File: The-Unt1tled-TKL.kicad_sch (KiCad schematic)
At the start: 194 parts, among them J1 USB_C_Receptacle_USB2.0, SW1 SW_Push, U1 ATmega32U4-A, Y1 16MHz

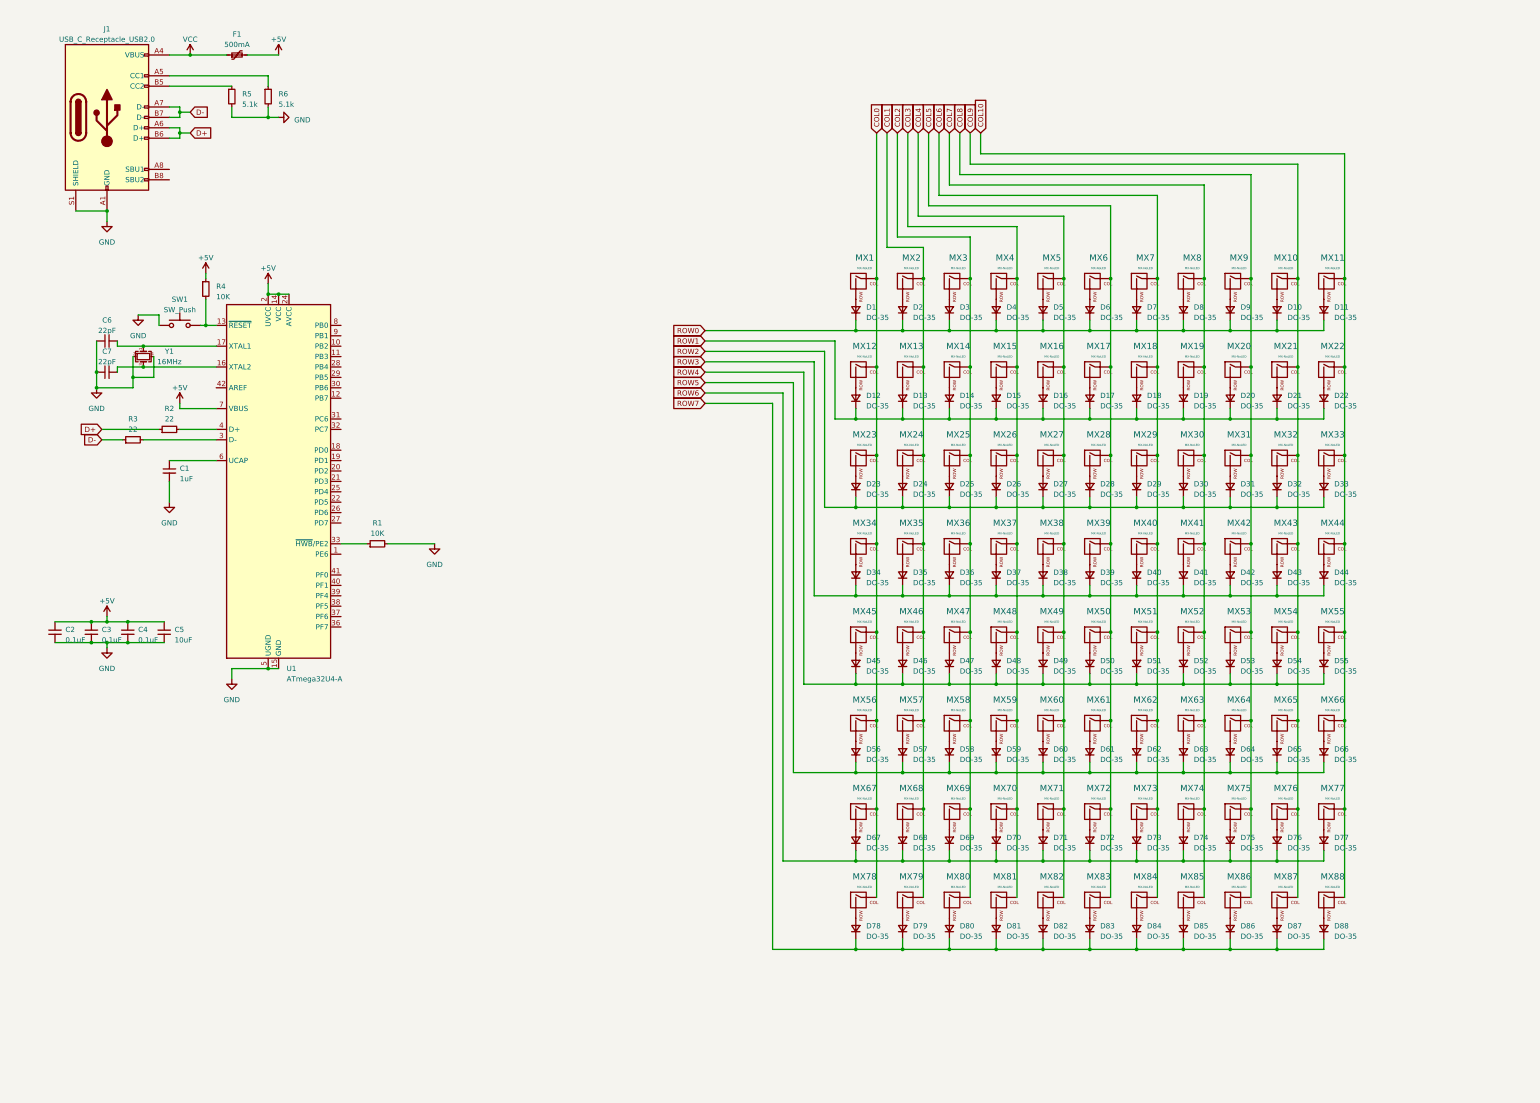
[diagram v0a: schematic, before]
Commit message: Re-did Whole Schematic
I redesigned the whole PCB schematic to support ISO and ANSI. I also changed the microcontroller to one with more pins for row/col layout. Instead I'm using an ATmega324A-P. This requires the use of v-usb.
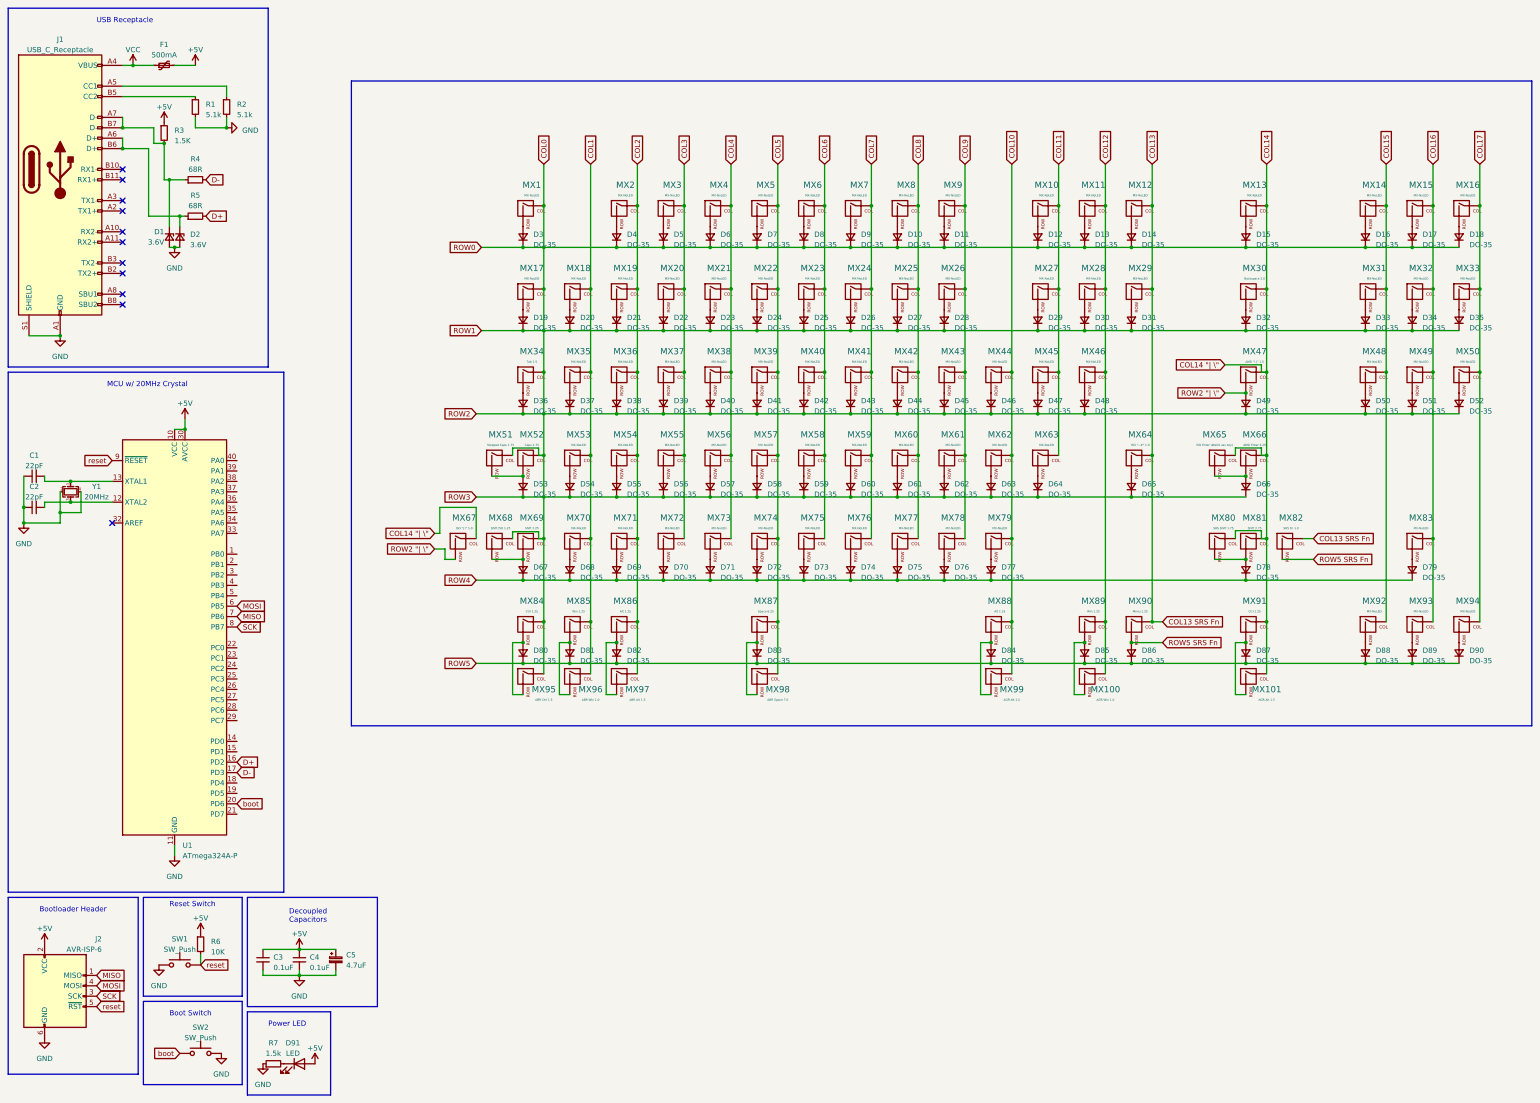
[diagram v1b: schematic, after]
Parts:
- removed C5: 10uF, Capacitor_THT:CP_Radial_D4.0mm_P1.50mm, symbol Device:C_Small
- removed C6, C7: 22pF, Capacitor_THT:C_Disc_D5.0mm_W2.5mm_P2.50mm, symbol Device:C_Small
- removed D1, D2: DO-35, Diode_THT:D_DO-35_SOD27_P7.62mm_Horizontal, symbol Device:D_Small
- removed J1: USB_C_Receptacle_USB2.0, Connector_USB:USB_C_Receptacle_G-Switch_GT-USB-7010ASV, symbol Connector:USB_C_Receptacle_USB2.0
- removed U1: ATmega32U4-A, Package_QFP:TQFP-44_10x10mm_P0.8mm, symbol MCU_Microchip_ATmega:ATmega32U4-A
- added C5: 4.7uF, symbol Device:C_Polarized_Small
- added D1, D2: 3.6V, symbol Device:D_Zener_Small
- added D89, D90: DO-35, Diode_THT:D_DO-35_SOD27_P7.62mm_Horizontal, symbol Device:D_Small
- added D91: LED, symbol Device:LED
- added J1: USB_C_Receptacle, symbol Connector:USB_C_Receptacle
- added J2: AVR-ISP-6, symbol Connector:AVR-ISP-6
- added MX100: AGR Win 1.0, MX_Alps_Hybrid:MX-1U-NoLED, symbol MX_Alps_Hybrid:MX-NoLED
- added MX101, MX99: AGR Alt 1.5, MX_Alps_Hybrid:MX-1U-NoLED, symbol MX_Alps_Hybrid:MX-NoLED
- added MX89: Win 1.25, MX_Alps_Hybrid:MX-1U-NoLED, symbol MX_Alps_Hybrid:MX-NoLED
- added MX90: Menu 1.25, MX_Alps_Hybrid:MX-1U-NoLED, symbol MX_Alps_Hybrid:MX-NoLED
- added MX91: Ctrl 1.25, MX_Alps_Hybrid:MX-1U-NoLED, symbol MX_Alps_Hybrid:MX-NoLED
- added MX92, MX93, MX94: MX-NoLED, MX_Alps_Hybrid:MX-1U-NoLED, symbol MX_Alps_Hybrid:MX-NoLED
- added MX95: ABR Ctrl 1.5, MX_Alps_Hybrid:MX-1U-NoLED, symbol MX_Alps_Hybrid:MX-NoLED
- added MX96: ABR Win 1.0, MX_Alps_Hybrid:MX-1U-NoLED, symbol MX_Alps_Hybrid:MX-NoLED
- added MX97: ABR Alt 1.5, MX_Alps_Hybrid:MX-1U-NoLED, symbol MX_Alps_Hybrid:MX-NoLED
- added MX98: ABR Space 7.0, MX_Alps_Hybrid:MX-1U-NoLED, symbol MX_Alps_Hybrid:MX-NoLED
- added R7: 1.5k, symbol Device:R_Small
- added SW2: SW_Push, symbol Switch:SW_Push
- added U1: ATmega324A-P, Package_DIP:DIP-40_W15.24mm, symbol MCU_Microchip_ATmega:ATmega324A-P
- C1: value 1uF -> 22pF; footprint Capacitor_THT:CP_Radial_D4.0mm_P1.50mm -> Capacitor_THT:C_Disc_D5.0mm_W2.5mm_P2.50mm
- C2: value 0.1uF -> 22pF; footprint Capacitor_THT:CP_Radial_D5.0mm_P2.00mm -> Capacitor_THT:C_Disc_D5.0mm_W2.5mm_P2.50mm
- MX30: value MX-NoLED -> Backspace 2.0
- MX34: value MX-NoLED -> Tab 1.5
- MX47: value MX-NoLED -> ANSI "\ |" 1.5
- MX51: value MX-NoLED -> Stepped Caps 1.75
- MX52: value MX-NoLED -> Caps 1.75
- MX64: value MX-NoLED -> ISO "~#" 1.0
- MX65: value MX-NoLED -> ISO Enter (Weird ass key)
- MX66: value MX-NoLED -> ANSI Enter 2.25
- MX67: value MX-NoLED -> ISO "| \" 1.0
- MX68: value MX-NoLED -> Shift ISO 1.25
- MX69: value MX-NoLED -> Shift 2.25
- MX73, MX74, MX75, MX76, MX77, MX78, MX79: footprint MX_Alps_Hybrid:MX-1.25U-NoLED -> MX_Alps_Hybrid:MX-1U-NoLED
- MX80: value MX-NoLED -> SRS Shift 1.75; footprint MX_Alps_Hybrid:MX-1.5U-NoLED -> MX_Alps_Hybrid:MX-1U-NoLED
- MX81: value MX-NoLED -> Shift 2.75; footprint MX_Alps_Hybrid:MX-1.5U-NoLED -> MX_Alps_Hybrid:MX-1U-NoLED
- MX82: value MX-NoLED -> SRS Fn 1.0; footprint MX_Alps_Hybrid:MX-1.75U-NoLED -> MX_Alps_Hybrid:MX-1U-NoLED
- MX83: footprint MX_Alps_Hybrid:MX-2U-NoLED -> MX_Alps_Hybrid:MX-1U-NoLED
- MX84: value MX-NoLED -> Ctrl 1.25; footprint MX_Alps_Hybrid:MX-2.25U-NoLED -> MX_Alps_Hybrid:MX-1U-NoLED
- MX85: value MX-NoLED -> Win 1.25; footprint MX_Alps_Hybrid:MX-2.25U-NoLED -> MX_Alps_Hybrid:MX-1U-NoLED
- MX86: value MX-NoLED -> Alt 1.25; footprint MX_Alps_Hybrid:MX-2.25U-NoLED -> MX_Alps_Hybrid:MX-1U-NoLED
- MX87: value MX-NoLED -> Space 6.25; footprint MX_Alps_Hybrid:MX-2.75U-NoLED -> MX_Alps_Hybrid:MX-1U-NoLED
- MX88: value MX-NoLED -> Alt 1.25; footprint MX_Alps_Hybrid:MX-6.25U-NoLED -> MX_Alps_Hybrid:MX-1U-NoLED
- R1: value 10K -> 5.1k
- R2: value 22 -> 5.1k
- R3: value 22 -> 1.5K; footprint Resistor_THT:R_Axial_DIN0207_L6.3mm_D2.5mm_P7.62mm_Horizontal -> (none)
- R4: value 10K -> 68R
- R5: value 5.1k -> 68R
- R6: value 5.1k -> 10K
- Y1: value 16MHz -> 20MHz
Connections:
- net ROW0 is gone; now on net COL0: D10.1 (K), D11.1 (K), D3.1 (K), D4.1 (K), D5.1 (K), D6.1 (K), D7.1 (K), D8.1 (K), D9.1 (K)
- net ROW1 is gone; now on net COL0: D12.1 (K), D13.1 (K), D14.1 (K), D15.1 (K), D16.1 (K), D17.1 (K), D18.1 (K), D19.1 (K), D20.1 (K), D21.1 (K), D22.1 (K)
- net ROW2 is gone; now on net COL0: D23.1 (K), D24.1 (K), D25.1 (K), D26.1 (K), D27.1 (K), D28.1 (K), D29.1 (K), D30.1 (K), D31.1 (K), D32.1 (K), D33.1 (K)
- net ROW3 is gone; now on net COL0: D34.1 (K), D35.1 (K), D36.1 (K), D37.1 (K), D38.1 (K), D39.1 (K), D40.1 (K), D41.1 (K), D42.1 (K), D43.1 (K), D44.1 (K)
- net ROW6 is gone; now on net ROW4: D67.1 (K), D68.1 (K), D69.1 (K), D70.1 (K), D71.1 (K), D72.1 (K), D73.1 (K), D74.1 (K), D75.1 (K), D76.1 (K), D77.1 (K)
- net +5V: now also R3.1, R6.1, C5.1, D91.2 (A), J2.2 (VCC), U1.10 (VCC), U1.30 (AVCC); no longer C2.1, R4.1
- net COL0: now also D45.1 (K), D46.1 (K), D47.1 (K), D48.1 (K), D49.1 (K), D50.1 (K), D51.1 (K), D52.1 (K), D53.1 (K), D54.1 (K), D55.1 (K), D56.1 (K), D57.1 (K), D58.1 (K), D59.1 (K), D60.1 (K), D61.1 (K), D62.1 (K), D63.1 (K), D64.1 (K), D65.1 (K), D66.1 (K), MX17.1 (COL), MX51.1 (COL), MX52.1 (COL), MX68.1 (COL), MX69.1 (COL), MX84.1 (COL), MX95.1 (COL); no longer MX12.1 (COL), MX23.1 (COL), MX45.1 (COL), MX56.1 (COL), MX67.1 (COL), MX78.1 (COL)
- net COL1: now also MX18.1 (COL), MX53.1 (COL), MX70.1 (COL), MX85.1 (COL), MX96.1 (COL); no longer MX13.1 (COL), MX2.1 (COL), MX24.1 (COL), MX46.1 (COL), MX57.1 (COL), MX68.1 (COL), MX79.1 (COL)
- net COL10: now also MX62.1 (COL), MX79.1 (COL), MX99.1 (COL); no longer MX11.1 (COL), MX22.1 (COL), MX33.1 (COL), MX55.1 (COL), MX66.1 (COL), MX77.1 (COL)
- net COL2: now also MX19.1 (COL), MX2.1 (COL), MX54.1 (COL), MX71.1 (COL), MX86.1 (COL), MX97.1 (COL); no longer MX14.1 (COL), MX25.1 (COL), MX3.1 (COL), MX47.1 (COL), MX58.1 (COL), MX69.1 (COL), MX80.1 (COL)
- net COL3: now also MX20.1 (COL), MX3.1 (COL), MX55.1 (COL), MX72.1 (COL); no longer MX15.1 (COL), MX26.1 (COL), MX4.1 (COL), MX48.1 (COL), MX59.1 (COL), MX70.1 (COL), MX81.1 (COL)
- net COL4: now also MX21.1 (COL), MX4.1 (COL), MX56.1 (COL), MX73.1 (COL); no longer MX16.1 (COL), MX27.1 (COL), MX49.1 (COL), MX5.1 (COL), MX60.1 (COL), MX71.1 (COL), MX82.1 (COL)
- net COL5: now also MX22.1 (COL), MX5.1 (COL), MX57.1 (COL), MX74.1 (COL), MX87.1 (COL), MX98.1 (COL); no longer MX17.1 (COL), MX28.1 (COL), MX50.1 (COL), MX6.1 (COL), MX61.1 (COL), MX72.1 (COL), MX83.1 (COL)
- net COL6: now also MX23.1 (COL), MX58.1 (COL), MX6.1 (COL), MX75.1 (COL); no longer MX18.1 (COL), MX29.1 (COL), MX51.1 (COL), MX62.1 (COL), MX7.1 (COL), MX73.1 (COL), MX84.1 (COL)
- net COL7: now also MX24.1 (COL), MX59.1 (COL), MX7.1 (COL), MX76.1 (COL); no longer MX19.1 (COL), MX30.1 (COL), MX52.1 (COL), MX63.1 (COL), MX74.1 (COL), MX8.1 (COL), MX85.1 (COL)
- net COL8: now also MX25.1 (COL), MX60.1 (COL), MX77.1 (COL), MX8.1 (COL); no longer MX20.1 (COL), MX31.1 (COL), MX53.1 (COL), MX64.1 (COL), MX75.1 (COL), MX86.1 (COL), MX9.1 (COL)
- net COL9: now also MX26.1 (COL), MX61.1 (COL), MX78.1 (COL), MX9.1 (COL); no longer MX10.1 (COL), MX21.1 (COL), MX32.1 (COL), MX54.1 (COL), MX65.1 (COL), MX76.1 (COL), MX87.1 (COL)
- net D+: now also R5.2, U1.16 (PD2); no longer R2.1
- net D-: now also R4.2, U1.17 (PD3); no longer R3.1
- net GND: now also C1.1, C2.1, R2.2, C5.2, D1.2 (A), D2.2 (A), J1.A1 (GND), J1.A12 (GND), J1.B1 (GND), J1.B12 (GND), J1.S1 (SHIELD), J2.6 (GND), R7.1, SW2.2, U1.11 (GND), U1.31 (GND); no longer C1.2, C2.2, R5.2, R6.2
- net ROW4: now also D78.1 (K), D79.1 (K); no longer D45.1 (K), D46.1 (K), D47.1 (K), D48.1 (K), D49.1 (K), D50.1 (K), D51.1 (K), D52.1 (K), D53.1 (K), D54.1 (K), D55.1 (K)
- net ROW5: now also D80.1 (K), D81.1 (K), D82.1 (K), D83.1 (K), D84.1 (K), D85.1 (K), D86.1 (K), D87.1 (K), D88.1 (K), D89.1 (K), D90.1 (K); no longer D56.1 (K), D57.1 (K), D58.1 (K), D59.1 (K), D60.1 (K), D61.1 (K), D62.1 (K), D63.1 (K), D64.1 (K), D65.1 (K), D66.1 (K)
- net VCC: now also J1.A4 (VBUS), J1.A9 (VBUS), J1.B4 (VBUS), J1.B9 (VBUS)
- net at MX40.2 (ROW): now also D42.2 (A); no longer D40.2 (A)
- net at D77.2 (A): now also MX79.2 (ROW); no longer MX77.2 (ROW)
- net at MX36.2 (ROW): now also D38.2 (A); no longer D36.2 (A)
- net at D61.2 (A): now also MX60.2 (ROW); no longer MX61.2 (ROW)
- net at D74.2 (A): now also MX76.2 (ROW); no longer MX74.2 (ROW)
- net at MX38.2 (ROW): now also D40.2 (A); no longer D38.2 (A)
- net at MX1.2 (ROW): now also D3.2 (A)
- net at MX58.2 (ROW): now also D59.2 (A); no longer D58.2 (A)
- net at D79.2 (A): now also MX83.2 (ROW); no longer MX79.2 (ROW)
- net at D6.2 (A): now also MX4.2 (ROW); no longer MX6.2 (ROW)
- net at D82.2 (A): now also MX86.2 (ROW), MX97.2 (ROW); no longer MX82.2 (ROW)
- net at D60.2 (A): now also MX59.2 (ROW); no longer MX60.2 (ROW)
- net at MX56.2 (ROW): now also D57.2 (A); no longer D56.2 (A)
- net at MX8.2 (ROW): now also D10.2 (A); no longer D8.2 (A)
- net at MX50.2 (ROW): now also D52.2 (A); no longer D50.2 (A)
- net at D83.2 (A): now also MX87.2 (ROW), MX98.2 (ROW); no longer MX83.2 (ROW)
- net at MX22.2 (ROW): now also D24.2 (A); no longer D22.2 (A)
- net at MX39.2 (ROW): now also D41.2 (A); no longer D39.2 (A)
- net at MX75.2 (ROW): now also D73.2 (A); no longer D75.2 (A)
- net at D47.2 (A): now also MX45.2 (ROW); no longer MX47.2 (ROW)
- net at MX43.2 (ROW): now also D45.2 (A); no longer D43.2 (A)
- net at MX10.2 (ROW): now also D12.2 (A); no longer D10.2 (A)
- net at D64.2 (A): now also MX63.2 (ROW); no longer MX64.2 (ROW)
- net at D81.2 (A): now also MX85.2 (ROW), MX96.2 (ROW); no longer MX81.2 (ROW)
- net at D46.2 (A): now also MX44.2 (ROW); no longer MX46.2 (ROW)
- net at MX41.2 (ROW): now also D43.2 (A); no longer D41.2 (A)
- net at MX24.2 (ROW): now also D26.2 (A); no longer D24.2 (A)
- net at MX14.2 (ROW): now also D16.2 (A); no longer D14.2 (A)
- net at D28.2 (A): now also MX26.2 (ROW); no longer MX28.2 (ROW)
- net at D9.2 (A): now also MX7.2 (ROW); no longer MX9.2 (ROW)
- net at MX35.2 (ROW): now also D37.2 (A); no longer D35.2 (A)
- net at MX17.2 (ROW): now also D19.2 (A); no longer D17.2 (A)
- net at MX73.2 (ROW): now also D71.2 (A); no longer D73.2 (A)
- net at MX42.2 (ROW): now also D44.2 (A); no longer D42.2 (A)
- net at MX57.2 (ROW): now also D58.2 (A); no longer D57.2 (A)
- net at R1.1: now also J1.B5 (CC2)
- net at D53.2 (A): now also MX51.2 (ROW), MX52.2 (ROW); no longer MX53.2 (ROW)
- net at MX27.2 (ROW): now also D29.2 (A); no longer D27.2 (A)
- net at MX33.2 (ROW): now also D35.2 (A); no longer D33.2 (A)
- net at D5.2 (A): now also MX3.2 (ROW); no longer MX5.2 (ROW)
- net at MX18.2 (ROW): now also D20.2 (A); no longer D18.2 (A)
- net at MX65.2 (ROW): now also D66.2 (A), MX66.2 (ROW); no longer D65.2 (A)
- net at D76.2 (A): now also MX78.2 (ROW); no longer MX76.2 (ROW)
- net at MX29.2 (ROW): now also D31.2 (A); no longer D29.2 (A)
- net at D4.2 (A): now also MX2.2 (ROW); no longer MX4.2 (ROW)
- net at MX31.2 (ROW): now also D33.2 (A); no longer D31.2 (A)
- net at D67.2 (A): now also MX68.2 (ROW), MX69.2 (ROW); no longer MX67.2 (ROW)
- net at D7.2 (A): now also MX5.2 (ROW); no longer MX7.2 (ROW)
- net at R3.2: now also R4.1, D1.1 (K), J1.A7 (D-), J1.B7 (D-)
- net at D34.2 (A): now also MX32.2 (ROW); no longer MX34.2 (ROW)
- net at MX55.2 (ROW): now also D56.2 (A); no longer D55.2 (A)
- net at D68.2 (A): now also MX70.2 (ROW); no longer MX68.2 (ROW)
- net at D63.2 (A): now also MX62.2 (ROW); no longer MX63.2 (ROW)
- net at D87.2 (A): now also MX101.2 (ROW), MX91.2 (ROW); no longer MX87.2 (ROW)
- net at D25.2 (A): now also MX23.2 (ROW); no longer MX25.2 (ROW)
- net at D85.2 (A): now also MX100.2 (ROW), MX89.2 (ROW); no longer MX85.2 (ROW)
- net reset: now reaches SW1.2
- net reset: now also R6.2, J2.5 (~{RST}), U1.9 (~{RESET}); no longer R4.2
- net at MX48.2 (ROW): now also D50.2 (A); no longer D48.2 (A)
- net at D70.2 (A): now also MX72.2 (ROW); no longer MX70.2 (ROW)
- net at MX16.2 (ROW): now also D18.2 (A); no longer D16.2 (A)
- net at R5.1: now also D2.1 (K), J1.A6 (D+), J1.B6 (D+)
- net at MX49.2 (ROW): now also D51.2 (A); no longer D49.2 (A)
- net at D32.2 (A): now also MX30.2 (ROW); no longer MX32.2 (ROW)
- net at MX37.2 (ROW): now also D39.2 (A); no longer D37.2 (A)
- net at MX71.2 (ROW): now also D69.2 (A); no longer D71.2 (A)
- net at MX19.2 (ROW): now also D21.2 (A); no longer D19.2 (A)
- net ROW5 SRS Fn: now reaches D86.2 (A)
- net ROW5 SRS Fn: now also MX82.2 (ROW), MX90.2 (ROW); no longer MX86.2 (ROW)
- net at D84.2 (A): now also MX88.2 (ROW), MX99.2 (ROW); no longer MX84.2 (ROW)
- net at MX20.2 (ROW): now also D22.2 (A); no longer D20.2 (A)
- net at D13.2 (A): now also MX11.2 (ROW); no longer MX13.2 (ROW)
- net at MX54.2 (ROW): now also D55.2 (A); no longer D54.2 (A)
- net at D30.2 (A): now also MX28.2 (ROW); no longer MX30.2 (ROW)
- net at MX80.2 (ROW): now also D78.2 (A), MX81.2 (ROW); no longer D80.2 (A)
- net at D88.2 (A): now also MX92.2 (ROW); no longer MX88.2 (ROW)
- net at MX21.2 (ROW): now also D23.2 (A); no longer D21.2 (A)
- net at MX15.2 (ROW): now also D17.2 (A); no longer D15.2 (A)
- net at MX12.2 (ROW): now also D14.2 (A); no longer D12.2 (A)
- net at D62.2 (A): now also MX61.2 (ROW); no longer MX62.2 (ROW)
- net at D11.2 (A): now also MX9.2 (ROW); no longer MX11.2 (ROW)
- net at D72.2 (A): now also MX74.2 (ROW); no longer MX72.2 (ROW)
- net at Y1.3: now also C2.2, U1.12 (XTAL2)
- net at Y1.1: now also C1.2, U1.13 (XTAL1)
- removed net ROW7: D78.1 (K), D79.1 (K), D80.1 (K), D81.1 (K), D82.1 (K), D83.1 (K), D84.1 (K), D85.1 (K), D86.1 (K), D87.1 (K), D88.1 (K)
- new net: D91.1 (K), R7.2
- new net: D90.2 (A), MX94.2 (ROW)
- new net: D80.2 (A), MX84.2 (ROW), MX95.2 (ROW)
- new net: D65.2 (A), MX64.2 (ROW)
- new net: D89.2 (A), MX93.2 (ROW)
- new net: D75.2 (A), MX77.2 (ROW)
- new net: J1.A5 (CC1), R2.1
- new net: D27.2 (A), MX25.2 (ROW)
- new net: D15.2 (A), MX13.2 (ROW)
- new net: D36.2 (A), MX34.2 (ROW)
- new net: D48.2 (A), MX46.2 (ROW)
- new net: D54.2 (A), MX53.2 (ROW)
- new net: D8.2 (A), MX6.2 (ROW)
- new net COL11: MX10.1 (COL), MX27.1 (COL), MX45.1 (COL), MX63.1 (COL)
- new net COL12: MX100.1 (COL), MX11.1 (COL), MX28.1 (COL), MX46.1 (COL), MX89.1 (COL)
- new net COL13: MX12.1 (COL), MX29.1 (COL), MX64.1 (COL), MX82.1 (COL), MX90.1 (COL)
- new net COL14: MX101.1 (COL), MX13.1 (COL), MX30.1 (COL), MX47.1 (COL), MX65.1 (COL), MX66.1 (COL), MX67.1 (COL), MX80.1 (COL), MX81.1 (COL), MX91.1 (COL)
- new net COL15: MX14.1 (COL), MX31.1 (COL), MX48.1 (COL), MX92.1 (COL)
- new net COL16: MX15.1 (COL), MX32.1 (COL), MX49.1 (COL), MX83.1 (COL), MX93.1 (COL)
- new net COL17: MX16.1 (COL), MX33.1 (COL), MX50.1 (COL), MX94.1 (COL)
- new net MISO: J2.1 (MISO), U1.7 (PB6)
- new net MOSI: J2.4 (MOSI), U1.6 (PB5)
- new net ROW2 "| \": D49.2 (A), MX47.2 (ROW), MX67.2 (ROW)
- new net SCK: J2.3 (SCK), U1.8 (PB7)
- new net boot: SW2.1, U1.20 (PD6)
- no-connect marks 0 -> 11
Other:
- note added: "Boot Switch"
- note added: "Bootloader Header"
- note added: "Decoupled Capacitors"
- note added: "MCU w/ 20MHz Crystal"
- note added: "Power LED"
- note added: "Reset Switch"
- note added: "USB Receptacle"

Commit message: Fuck PCB Grid Editor
I'm gonna put a bullet in my head.
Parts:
- C5: footprint (none) -> Capacitor_THT:CP_Radial_D5.0mm_P2.00mm
- D1, D2: footprint (none) -> Diode_THT:D_DO-35_SOD27_P7.62mm_Horizontal
- D91: value LED -> Power LED; footprint (none) -> LED_SMD:LED_2010_5025Metric_Pad1.52x2.65mm_HandSolder
- J1: footprint (none) -> Connector_USB:USB_C_Receptacle_Amphenol_12401548E4-2A
- J2: footprint (none) -> Connector_IDC:IDC-Header_2x03_P2.54mm_Vertical
- MX1: value MX-NoLED -> ESC
- MX10: value MX-NoLED -> F9
- MX100: value AGR Win 1.0 -> ABR Right Win 1.0
- MX101: value AGR Alt 1.5 -> ABR Right Ctrl 1.5; footprint MX_Alps_Hybrid:MX-1U-NoLED -> MX_Alps_Hybrid:MX-1.5U-NoLED
- MX11: value MX-NoLED -> F10
- MX12: value MX-NoLED -> F11
- MX13: value MX-NoLED -> F12
- MX14: value MX-NoLED -> PrtSc
- MX15: value MX-NoLED -> Scroll Lock
- MX16: value MX-NoLED -> Pause/Break
- MX17: value MX-NoLED -> Tilde
- MX18: value MX-NoLED -> 1
- MX19: value MX-NoLED -> 2
- MX2: value MX-NoLED -> F1
- MX20: value MX-NoLED -> 3
- MX21: value MX-NoLED -> 4
- MX22: value MX-NoLED -> 5
- MX23: value MX-NoLED -> 6
- MX24: value MX-NoLED -> 7
- MX25: value MX-NoLED -> 8
- MX26: value MX-NoLED -> 9
- MX27: value MX-NoLED -> 0
- MX28: value MX-NoLED -> Minus
- MX29: value MX-NoLED -> Plus
- MX3: value MX-NoLED -> F2
- MX30: footprint MX_Alps_Hybrid:MX-1U-NoLED -> MX_Alps_Hybrid:MX-2U-NoLED
- MX31: value MX-NoLED -> Insert
- MX32: value MX-NoLED -> Home
- MX33: value MX-NoLED -> PgUp
- MX34, MX47: footprint MX_Alps_Hybrid:MX-1U-NoLED -> MX_Alps_Hybrid:MX-1.5U-NoLED
- MX35: value MX-NoLED -> Q
- MX36: value MX-NoLED -> W
- MX37: value MX-NoLED -> E
- MX38: value MX-NoLED -> R
- MX39: value MX-NoLED -> T
- MX4: value MX-NoLED -> F3
- MX40: value MX-NoLED -> Y
- MX41: value MX-NoLED -> U
- MX42: value MX-NoLED -> I
- MX43: value MX-NoLED -> O
- MX44: value MX-NoLED -> P
- MX45: value MX-NoLED -> [
- MX46: value MX-NoLED -> ]
- MX48: value MX-NoLED -> Delete
- MX49: value MX-NoLED -> End
- MX5: value MX-NoLED -> F4
- MX50: value MX-NoLED -> PgDn
- MX51: value Stepped Caps 1.75 -> Stepped Caps 1.25; footprint MX_Alps_Hybrid:MX-1U-NoLED -> MX_Alps_Hybrid:MX-1.25U-NoLED
- MX52: footprint MX_Alps_Hybrid:MX-1U-NoLED -> MX_Alps_Hybrid:MX-1.75U-NoLED
- MX53: value MX-NoLED -> A
- MX54: value MX-NoLED -> S
- MX55: value MX-NoLED -> D
- MX56: value MX-NoLED -> F
- MX57: value MX-NoLED -> G
- MX58: value MX-NoLED -> H
- MX59: value MX-NoLED -> J
- MX6: value MX-NoLED -> F5
- MX60: value MX-NoLED -> K
- MX61: value MX-NoLED -> L
- MX62: value MX-NoLED -> Semicolon
- MX63: value MX-NoLED -> Apostrophe
- MX65: footprint MX_Alps_Hybrid:MX-1U-NoLED -> MX_Alps_Hybrid:MX-ISO
- MX66: footprint MX_Alps_Hybrid:MX-1U-NoLED -> MX_Alps_Hybrid:MX-2.25U-NoLED
- MX68: value Shift ISO 1.25 -> Left Shift ISO 1.25; footprint MX_Alps_Hybrid:MX-1U-NoLED -> MX_Alps_Hybrid:MX-1.25U-NoLED
- MX69: value Shift 2.25 -> Left Shift 2.25; footprint MX_Alps_Hybrid:MX-1U-NoLED -> MX_Alps_Hybrid:MX-2.25U-NoLED
- MX7: value MX-NoLED -> F6
- MX70: value MX-NoLED -> Z
- MX71: value MX-NoLED -> X
- MX72: value MX-NoLED -> C
- MX73: value MX-NoLED -> V
- MX74: value MX-NoLED -> B
- MX75: value MX-NoLED -> N
- MX76: value MX-NoLED -> M
- MX77: value MX-NoLED -> Comma
- MX78: value MX-NoLED -> Period
- MX79: value MX-NoLED -> Question
- MX8: value MX-NoLED -> F7
- MX80: value SRS Shift 1.75 -> SRS Right Shift 1.75; footprint MX_Alps_Hybrid:MX-1U-NoLED -> MX_Alps_Hybrid:MX-1.75U-NoLED
- MX81: value Shift 2.75 -> Right Shift 2.75; footprint MX_Alps_Hybrid:MX-1U-NoLED -> MX_Alps_Hybrid:MX-2.75U-NoLED
- MX83: value MX-NoLED -> Up Arrow
- MX84: value Ctrl 1.25 -> Left Ctrl 1.25; footprint MX_Alps_Hybrid:MX-1U-NoLED -> MX_Alps_Hybrid:MX-1.25U-NoLED
- MX85: value Win 1.25 -> Left Win 1.25; footprint MX_Alps_Hybrid:MX-1U-NoLED -> MX_Alps_Hybrid:MX-1.25U-NoLED
- MX86: value Alt 1.25 -> Left Alt 1.25; footprint MX_Alps_Hybrid:MX-1U-NoLED -> MX_Alps_Hybrid:MX-1.25U-NoLED
- MX87: footprint MX_Alps_Hybrid:MX-1U-NoLED -> MX_Alps_Hybrid:MX-6.25U-NoLED
- MX88: value Alt 1.25 -> Right Alt 1.25; footprint MX_Alps_Hybrid:MX-1U-NoLED -> MX_Alps_Hybrid:MX-1.25U-NoLED
- MX89: value Win 1.25 -> RightWin 1.25; footprint MX_Alps_Hybrid:MX-1U-NoLED -> MX_Alps_Hybrid:MX-1.25U-NoLED
- MX9: value MX-NoLED -> F8
- MX90: footprint MX_Alps_Hybrid:MX-1U-NoLED -> MX_Alps_Hybrid:MX-1.25U-NoLED
- MX91: value Ctrl 1.25 -> Right Ctrl 1.25; footprint MX_Alps_Hybrid:MX-1U-NoLED -> MX_Alps_Hybrid:MX-1.25U-NoLED
- MX92: value MX-NoLED -> Left Arrow
- MX93: value MX-NoLED -> Down Arrow
- MX94: value MX-NoLED -> Right Arrow
- MX95: value ABR Ctrl 1.5 -> ABR Left Ctrl 1.5; footprint MX_Alps_Hybrid:MX-1U-NoLED -> MX_Alps_Hybrid:MX-1.5U-NoLED
- MX96: value ABR Win 1.0 -> ABR Left Win 1.0
- MX97: value ABR Alt 1.5 -> ABR Left Alt 1.5; footprint MX_Alps_Hybrid:MX-1U-NoLED -> MX_Alps_Hybrid:MX-1.5U-NoLED
- MX98: footprint MX_Alps_Hybrid:MX-1U-NoLED -> MX_Alps_Hybrid:MX-7U-NoLED
- MX99: value AGR Alt 1.5 -> ABR Right Alt 1.5; footprint MX_Alps_Hybrid:MX-1U-NoLED -> MX_Alps_Hybrid:MX-1.5U-NoLED
- R3, R7: footprint (none) -> Resistor_THT:R_Axial_DIN0207_L6.3mm_D2.5mm_P7.62mm_Horizontal
- SW1: value SW_Push -> SW_Reset
- SW2: value SW_Push -> SW_Boot; footprint (none) -> random-keyboard-parts:SKQG-1155865
- U1: footprint Package_DIP:DIP-40_W15.24mm -> Package_DIP:DIP-40_W15.24mm_Socket_LongPads

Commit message: Many things
- Figured out grid placement
- Working on part placements
- Changed footprint from MX-Alp Hybrid to MX-Only.
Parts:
- MX1, MX10, MX100, MX11, MX12, MX13, MX14, MX15, MX16, MX17, MX18, MX19, MX2, MX20, MX21, MX22, MX23, MX24, MX25, MX26, MX27, MX28, MX29, MX3, MX31, MX32, MX33, MX35, MX36, MX37, MX38, MX39, MX4, MX40, MX41, MX42, MX43, MX44, MX45, MX46, MX48, MX49, MX5, MX50, MX53, MX54, MX55, MX56, MX57, MX58, MX59, MX6, MX60, MX61, MX62, MX63, MX64, MX67, MX7, MX70, MX71, MX72, MX73, MX74, MX75, MX76, MX77, MX78, MX79, MX8, MX82, MX83, MX9, MX92, MX93, MX94, MX96: footprint MX_Alps_Hybrid:MX-1U-NoLED -> MX_Only:MXOnly-1U-NoLED
- MX101, MX34, MX47, MX95, MX97, MX99: footprint MX_Alps_Hybrid:MX-1.5U-NoLED -> MX_Only:MXOnly-1.5U-NoLED
- MX30: footprint MX_Alps_Hybrid:MX-2U-NoLED -> MX_Only:MXOnly-1U-NoLED
- MX51, MX68, MX84, MX85, MX86, MX88, MX89, MX90, MX91: footprint MX_Alps_Hybrid:MX-1.25U-NoLED -> MX_Only:MXOnly-1.25U-NoLED
- MX52, MX80: footprint MX_Alps_Hybrid:MX-1.75U-NoLED -> MX_Only:MXOnly-1.75U-NoLED
- MX65: footprint MX_Alps_Hybrid:MX-ISO -> MX_Only:MXOnly-ISO-NoLED
- MX66, MX69: footprint MX_Alps_Hybrid:MX-2.25U-NoLED -> MX_Only:MXOnly-2.25U-NoLED
- MX81: footprint MX_Alps_Hybrid:MX-2.75U-NoLED -> MX_Only:MXOnly-2.75U-NoLED
- MX87: footprint MX_Alps_Hybrid:MX-6.25U-NoLED -> MX_Only:MXOnly-6.25U-NoLED
- MX98: footprint MX_Alps_Hybrid:MX-7U-NoLED -> MX_Only:MXOnly-7U-NoLED
